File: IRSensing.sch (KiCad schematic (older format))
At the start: 0 parts

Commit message: Adding IR Sensor
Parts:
- added R11, R12: R, symbol R
- added U3: OPB733TR, Custom:OPB733TR, symbol OPB733TR
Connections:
- new net: R12.1, U3.4 (AN)
- new net +5V: R11.2, R12.2
- new net GND: U3.1 (CAT), U3.2 (E)
- new net Vout_IR: R11.1, U3.3 (C)
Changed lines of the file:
@@
 Comment4 ""
 $EndDescr
+$Comp
+L OPB733TR U3
+U 1 1 5AA80AD0
+P 5600 3350
+F 0 "U3" H 5600 3050 60  0000 C CNN
+F 1 "OPB733TR" H 5600 3650 60  0000 C CNN
+F 2 "Custom:OPB733TR" H 5500 2950 60  0001 C CNN
+F 3 "http://www.ttelectronics.com/sites/default/files/download-files/OPB733TR.pdf" H 5600 2950 60  0001 C CNN
+	1    5600 3350
+	-1   0    0    1
+$EndComp
+Wire Wire Line
+	6150 3450 6350 3450
+Wire Wire Line
+	6350 3450 6350 3000
+Wire Wire Line
+	6150 3250 6350 3250
+Connection ~ 6350 3250
+$Comp
+L R R11
+U 1 1 5AA80B31
+P 4750 3250
+F 0 "R11" V 4830 3250 50  0000 C CNN
+F 1 "R" V 4750 3250 50  0000 C CNN
+F 2 "" V 4680 3250 50  0001 C CNN
+F 3 "" H 4750 3250 50  0001 C CNN
+	1    4750 3250
+	0    1    1    0
+$EndComp
+$Comp
+L R R12
+U 1 1 5AA80B73
+P 4750 3450
+F 0 "R12" V 4830 3450 50  0000 C CNN
+F 1 "R" V 4750 3450 50  0000 C CNN
+F 2 "" V 4680 3450 50  0001 C CNN
+F 3 "" H 4750 3450 50  0001 C CNN
+	1    4750 3450
+	0    1    1    0
+$EndComp
+Wire Wire Line
+	4900 3250 5050 3250
+Wire Wire Line
+	5050 3450 4900 3450
+Wire Wire Line
+	4600 3450 4350 3450
+Wire Wire Line
+	4350 3450 4350 3000
+Wire Wire Line
+	4350 3250 4600 3250
+Connection ~ 4350 3250
+$Comp
+L +5V #PWR017
+U 1 1 5AA80C09
+P 4350 3000
+F 0 "#PWR017" H 4350 2850 50  0001 C CNN
+F 1 "+5V" H 4350 3140 50  0000 C CNN
+F 2 "" H 4350 3000 50  0001 C CNN
+F 3 "" H 4350 3000 50  0001 C CNN
+	1    4350 3000
+	1    0    0    -1
+$EndComp
+$Comp
+L GND #PWR018
+U 1 1 5AA80C23
+P 6350 3000
+F 0 "#PWR018" H 6350 2750 50  0001 C CNN
+F 1 "GND" H 6350 2850 50  0000 C CNN
+F 2 "" H 6350 3000 50  0001 C CNN
+F 3 "" H 6350 3000 50  0001 C CNN
+	1    6350 3000
+	-1   0    0    1
+$EndComp
+Text HLabel 5000 3100 1    60   Output Italic 0
+Vout_IR
+Wire Wire Line
+	5000 3100 5000 3250
+Connection ~ 5000 3250
 $EndSCHEMATC

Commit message: Finished Schematic
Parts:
- added J? (x8): Conn_01x03, symbol Conn_01x03
- added Q?: Q_NPN_BEC, symbol Q_NPN_BEC
- added R? (x3): 30k, symbol R
- added R? (x3): 36, symbol R
- added U? (x3): OPB733TR, Custom:OPB733TR, symbol OPB733TR
- R?: renamed from R11; value R -> 30k
- R?: renamed from R12; value R -> 36
- renumbered U3 to U?
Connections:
- net GND: now also J?.1 (Pin_1), J?.1 (Pin_1), J?.1 (Pin_1), J?.1 (Pin_1); no longer U?.1 (CAT), U?.2 (E)
- net +5V renamed 3V3_C1
- net 3V3_C1: now also J?.2 (Pin_2)
- net Vout_IR renamed Vout_IR_C1
- net Vout_IR_C1: now also J?.3 (Pin_3)
- new net: R?.1, U?.4 (AN) (x3)
- new net +3V3: Q?.3 (C)
- new net 3V3_C2: J?.2 (Pin_2), R?.2, R?.2
- new net 3V3_C3: J?.2 (Pin_2), R?.2, R?.2
- new net 3V3_C4: J?.2 (Pin_2), R?.2, R?.2
- new net D_Power: J?.2 (Pin_2), J?.2 (Pin_2), J?.2 (Pin_2), J?.2 (Pin_2), Q?.2 (E)
- new net D_SIG: Q?.1 (B)
- new net GND_C1: J?.1 (Pin_1), U?.1 (CAT), U?.2 (E)
- new net GND_C2: J?.1 (Pin_1), U?.1 (CAT), U?.2 (E)
- new net GND_C3: J?.1 (Pin_1), U?.1 (CAT), U?.2 (E)
- new net GND_C4: J?.1 (Pin_1), U?.1 (CAT), U?.2 (E)
- new net Vout_IR_1: J?.3 (Pin_3)
- new net Vout_IR_2: J?.3 (Pin_3)
- new net Vout_IR_3: J?.3 (Pin_3)
- new net Vout_IR_4: J?.3 (Pin_3)
- new net Vout_IR_C2: J?.3 (Pin_3), R?.1, U?.3 (C)
- new net Vout_IR_C3: J?.3 (Pin_3), R?.1, U?.3 (C)
- new net Vout_IR_C4: J?.3 (Pin_3), R?.1, U?.3 (C)
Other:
- note added: "Diode Power"
- note added: "IR Boards"
- note added: "Main Board"
- moved on the sheet: R?, U?

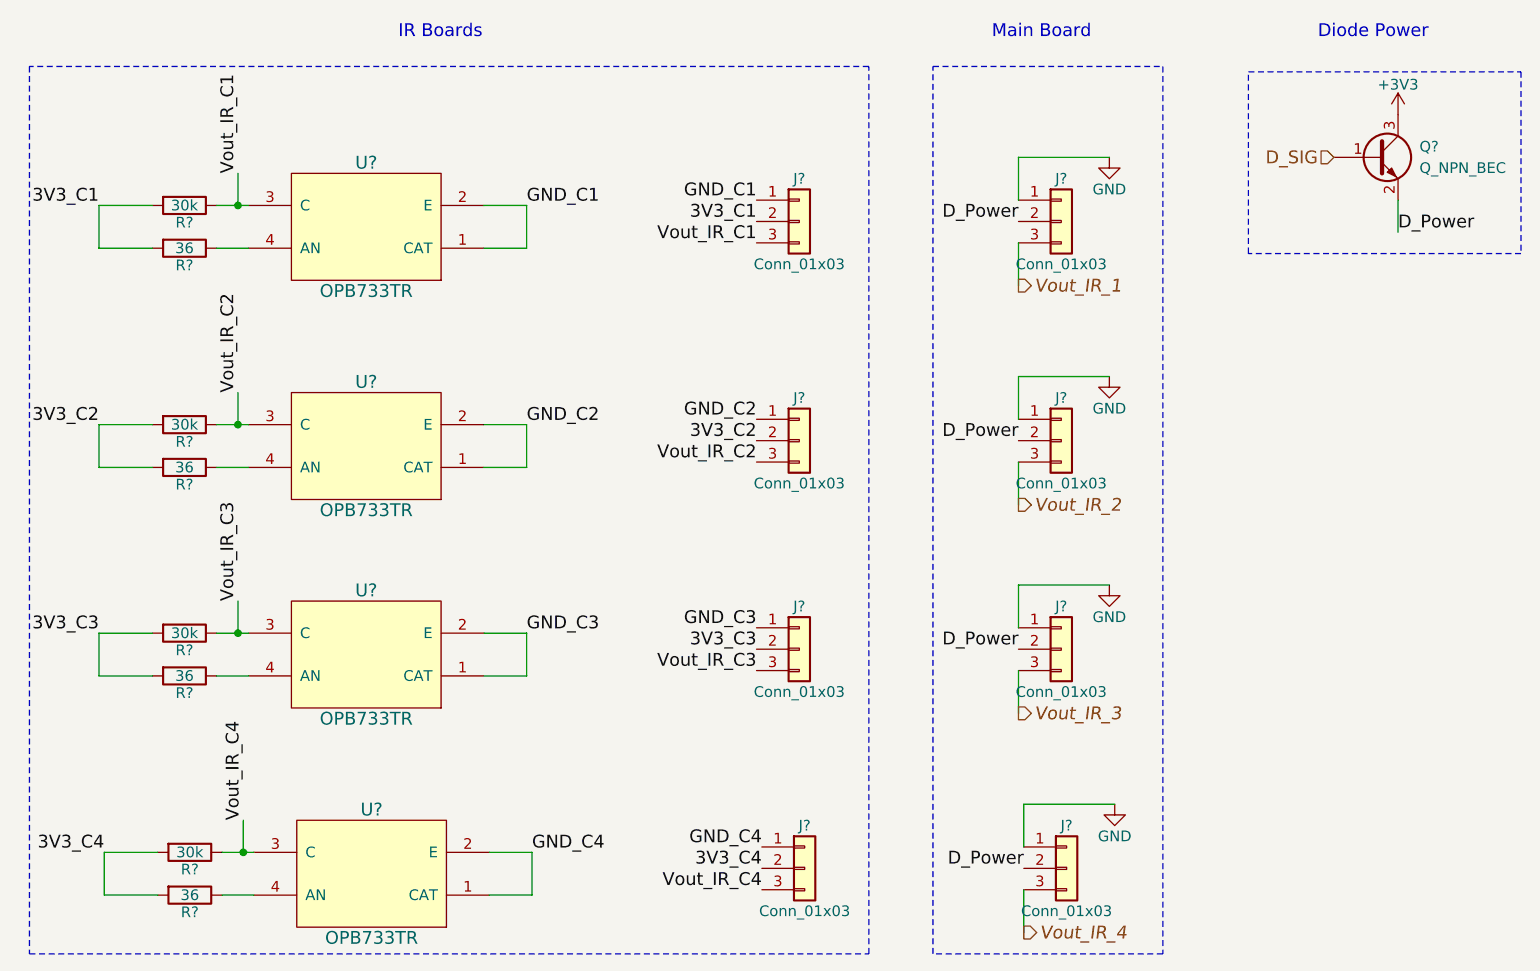
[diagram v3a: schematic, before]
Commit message: Started associating footprints
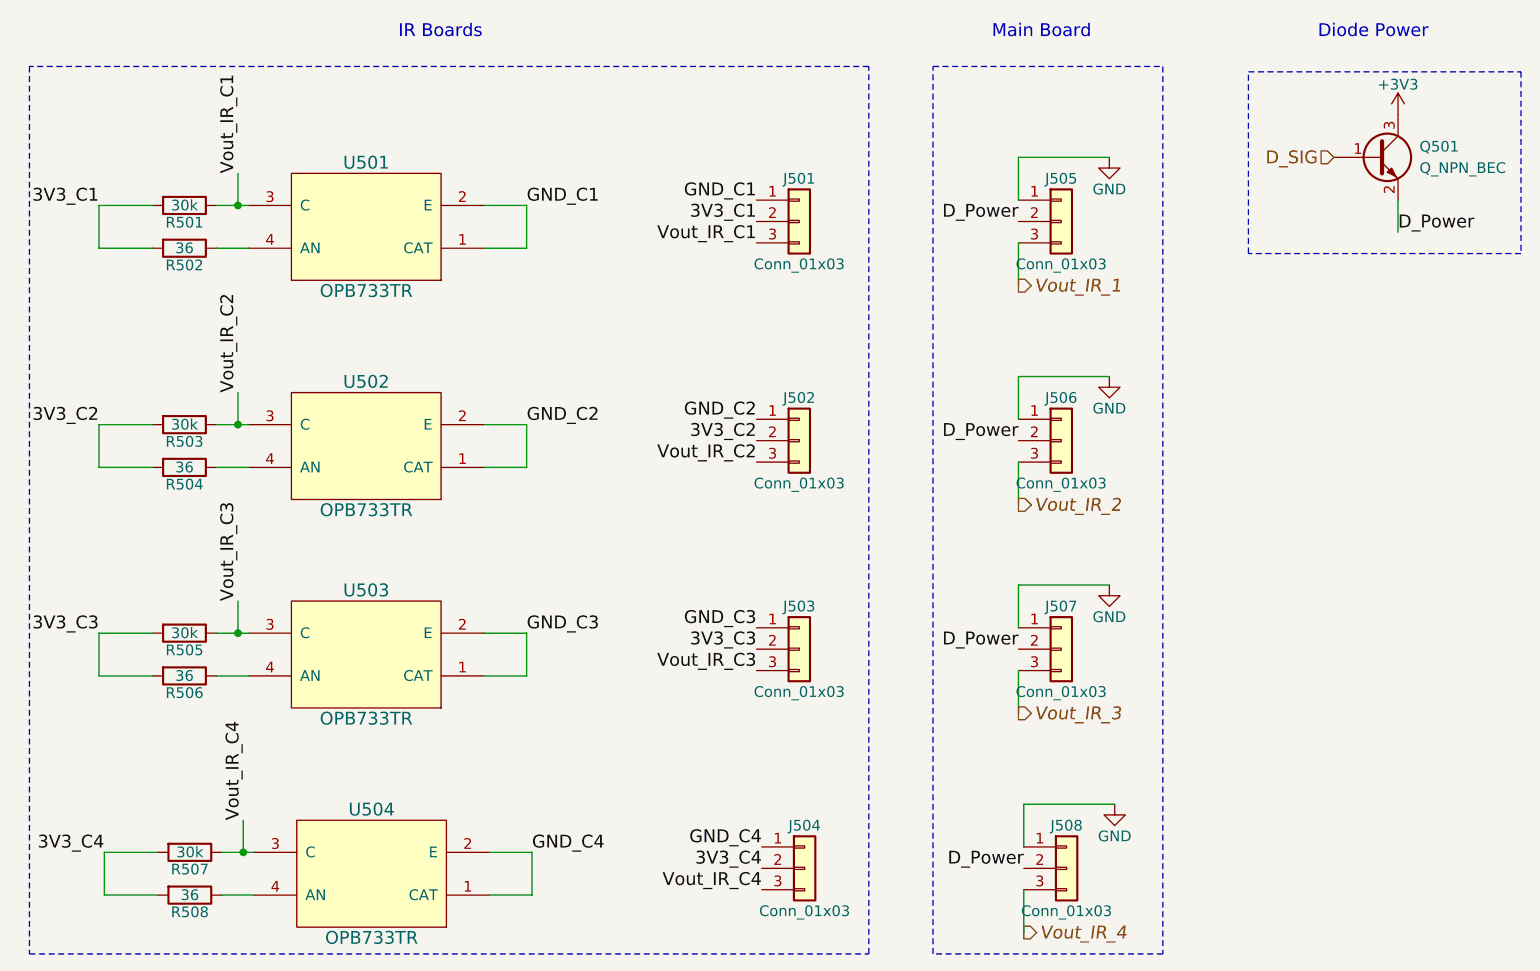
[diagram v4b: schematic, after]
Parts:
- J501, J502, J503, J504, J505, J506, J507, J508: renamed from J?; footprint (none) -> Pin_Headers:Pin_Header_Angled_1x03_Pitch1.27mm
- gave numbers to parts that had none: 13
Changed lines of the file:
@@
 $EndDescr
 $Comp
-L OPB733TR U?
+L OPB733TR U501
 U 1 1 5AA80AD0
 P 3125 2125
-F 0 "U?" H 3125 1825 60  0000 C CNN
+F 0 "U501" H 3125 1825 60  0000 C CNN
 F 1 "OPB733TR" H 3125 2425 60  0000 C CNN
 F 2 "Custom:OPB733TR" H 3025 1725 60  0001 C CNN
@@
 	3675 2025 3875 2025
 $Comp
-L R R?
+L R R501
 U 1 1 5AA80B31
 P 2275 2025
-F 0 "R?" V 2355 2025 50  0000 C CNN
+F 0 "R501" V 2355 2025 50  0000 C CNN
 F 1 "30k" V 2275 2025 50  0000 C CNN
 F 2 "" V 2205 2025 50  0001 C CNN
@@
 $EndComp
 $Comp
-L R R?
+L R R502
 U 1 1 5AA80B73
 P 2275 2225
-F 0 "R?" V 2355 2225 50  0000 C CNN
+F 0 "R502" V 2355 2225 50  0000 C CNN
 F 1 "36" V 2275 2225 50  0000 C CNN
 F 2 "" V 2205 2225 50  0001 C CNN
@@
 	1875 2025 2125 2025
 $Comp
-L GND #PWR018
+L GND #PWR029
 U 1 1 5AA80C23
 P 6600 1800
-F 0 "#PWR018" H 6600 1550 50  0001 C CNN
+F 0 "#PWR029" H 6600 1550 50  0001 C CNN
 F 1 "GND" H 6600 1650 50  0000 C CNN
 F 2 "" H 6600 1800 50  0001 C CNN
@@
 Connection ~ 2525 2025
 $Comp
-L Conn_01x03 J?
+L Conn_01x03 J501
 U 1 1 5AC5CFBC
 P 5150 2100
-F 0 "J?" H 5150 2300 50  0000 C CNN
+F 0 "J501" H 5150 2300 50  0000 C CNN
 F 1 "Conn_01x03" H 5150 1900 50  0000 C CNN
-F 2 "" H 5150 2100 50  0001 C CNN
+F 2 "Pin_Headers:Pin_Header_Angled_1x03_Pitch1.27mm" H 5150 2100 50  0001 C CNN
 F 3 "" H 5150 2100 50  0001 C CNN
 	1    5150 2100
@@
 3V3_C1
 $Comp
-L Conn_01x03 J?
+L Conn_01x03 J505
 U 1 1 5AC5E221
 P 6375 2100
-F 0 "J?" H 6375 2300 50  0000 C CNN
+F 0 "J505" H 6375 2300 50  0000 C CNN
 F 1 "Conn_01x03" H 6375 1900 50  0000 C CNN
-F 2 "" H 6375 2100 50  0001 C CNN
+F 2 "Pin_Headers:Pin_Header_Angled_1x03_Pitch1.27mm" H 6375 2100 50  0001 C CNN
 F 3 "" H 6375 2100 50  0001 C CNN
 	1    6375 2100
@@
 	1875 2225 1875 2025
 $Comp
-L OPB733TR U?
+L OPB733TR U502
 U 1 1 5AC5EDE3
 P 3125 3150
-F 0 "U?" H 3125 2850 60  0000 C CNN
+F 0 "U502" H 3125 2850 60  0000 C CNN
 F 1 "OPB733TR" H 3125 3450 60  0000 C CNN
 F 2 "Custom:OPB733TR" H 3025 2750 60  0001 C CNN
@@
 	3675 3050 3875 3050
 $Comp
-L R R?
+L R R503
 U 1 1 5AC5EDEB
 P 2275 3050
-F 0 "R?" V 2355 3050 50  0000 C CNN
+F 0 "R503" V 2355 3050 50  0000 C CNN
 F 1 "30k" V 2275 3050 50  0000 C CNN
 F 2 "" V 2205 3050 50  0001 C CNN
@@
 $EndComp
 $Comp
-L R R?
+L R R504
 U 1 1 5AC5EDF1
 P 2275 3250
-F 0 "R?" V 2355 3250 50  0000 C CNN
+F 0 "R504" V 2355 3250 50  0000 C CNN
 F 1 "36" V 2275 3250 50  0000 C CNN
 F 2 "" V 2205 3250 50  0001 C CNN
@@
 	1875 3050 2125 3050
 $Comp
-L GND #PWR?
+L GND #PWR030
 U 1 1 5AC5EDFB
 P 6600 2825
-F 0 "#PWR?" H 6600 2575 50  0001 C CNN
+F 0 "#PWR030" H 6600 2575 50  0001 C CNN
 F 1 "GND" H 6600 2675 50  0000 C CNN
 F 2 "" H 6600 2825 50  0001 C CNN
@@
 Connection ~ 2525 3050
 $Comp
-L Conn_01x03 J?
+L Conn_01x03 J502
 U 1 1 5AC5EE0A
 P 5150 3125
-F 0 "J?" H 5150 3325 50  0000 C CNN
+F 0 "J502" H 5150 3325 50  0000 C CNN
 F 1 "Conn_01x03" H 5150 2925 50  0000 C CNN
-F 2 "" H 5150 3125 50  0001 C CNN
+F 2 "Pin_Headers:Pin_Header_Angled_1x03_Pitch1.27mm" H 5150 3125 50  0001 C CNN
 F 3 "" H 5150 3125 50  0001 C CNN
 	1    5150 3125
@@
 3V3_C2
 $Comp
-L Conn_01x03 J?
+L Conn_01x03 J506
 U 1 1 5AC5EE16
 P 6375 3125
-F 0 "J?" H 6375 3325 50  0000 C CNN
+F 0 "J506" H 6375 3325 50  0000 C CNN
 F 1 "Conn_01x03" H 6375 2925 50  0000 C CNN
-F 2 "" H 6375 3125 50  0001 C CNN
+F 2 "Pin_Headers:Pin_Header_Angled_1x03_Pitch1.27mm" H 6375 3125 50  0001 C CNN
 F 3 "" H 6375 3125 50  0001 C CNN
 	1    6375 3125
@@
 	1875 3250 1875 3050
 $Comp
-L OPB733TR U?
+L OPB733TR U503
 U 1 1 5AC5EFD0
 P 3125 4125
-F 0 "U?" H 3125 3825 60  0000 C CNN
+F 0 "U503" H 3125 3825 60  0000 C CNN
 F 1 "OPB733TR" H 3125 4425 60  0000 C CNN
 F 2 "Custom:OPB733TR" H 3025 3725 60  0001 C CNN
@@
 	3675 4025 3875 4025
 $Comp
-L R R?
+L R R505
 U 1 1 5AC5EFD8
 P 2275 4025
-F 0 "R?" V 2355 4025 50  0000 C CNN
+F 0 "R505" V 2355 4025 50  0000 C CNN
 F 1 "30k" V 2275 4025 50  0000 C CNN
 F 2 "" V 2205 4025 50  0001 C CNN
@@
 $EndComp
 $Comp
-L R R?
+L R R506
 U 1 1 5AC5EFDE
 P 2275 4225
-F 0 "R?" V 2355 4225 50  0000 C CNN
+F 0 "R506" V 2355 4225 50  0000 C CNN
 F 1 "36" V 2275 4225 50  0000 C CNN
 F 2 "" V 2205 4225 50  0001 C CNN
@@
 	1875 4025 2125 4025
 $Comp
-L GND #PWR?
+L GND #PWR031
 U 1 1 5AC5EFE8
 P 6600 3800
-F 0 "#PWR?" H 6600 3550 50  0001 C CNN
+F 0 "#PWR031" H 6600 3550 50  0001 C CNN
 F 1 "GND" H 6600 3650 50  0000 C CNN
 F 2 "" H 6600 3800 50  0001 C CNN
@@
 Connection ~ 2525 4025
 $Comp
-L Conn_01x03 J?
+L Conn_01x03 J503
 U 1 1 5AC5EFF7
 P 5150 4100
-F 0 "J?" H 5150 4300 50  0000 C CNN
+F 0 "J503" H 5150 4300 50  0000 C CNN
 F 1 "Conn_01x03" H 5150 3900 50  0000 C CNN
-F 2 "" H 5150 4100 50  0001 C CNN
+F 2 "Pin_Headers:Pin_Header_Angled_1x03_Pitch1.27mm" H 5150 4100 50  0001 C CNN
 F 3 "" H 5150 4100 50  0001 C CNN
 	1    5150 4100
@@
 3V3_C3
 $Comp
-L Conn_01x03 J?
+L Conn_01x03 J507
 U 1 1 5AC5F003
 P 6375 4100
-F 0 "J?" H 6375 4300 50  0000 C CNN
+F 0 "J507" H 6375 4300 50  0000 C CNN
 F 1 "Conn_01x03" H 6375 3900 50  0000 C CNN
-F 2 "" H 6375 4100 50  0001 C CNN
+F 2 "Pin_Headers:Pin_Header_Angled_1x03_Pitch1.27mm" H 6375 4100 50  0001 C CNN
 F 3 "" H 6375 4100 50  0001 C CNN
 	1    6375 4100
@@
 	1875 4225 1875 4025
 $Comp
-L OPB733TR U?
+L OPB733TR U504
 U 1 1 5AC5F0CD
 P 3150 5150
-F 0 "U?" H 3150 4850 60  0000 C CNN
+F 0 "U504" H 3150 4850 60  0000 C CNN
 F 1 "OPB733TR" H 3150 5450 60  0000 C CNN
 F 2 "Custom:OPB733TR" H 3050 4750 60  0001 C CNN
@@
 	3700 5050 3900 5050
 $Comp
-L R R?
+L R R507
 U 1 1 5AC5F0D5
 P 2300 5050
-F 0 "R?" V 2380 5050 50  0000 C CNN
+F 0 "R507" V 2380 5050 50  0000 C CNN
 F 1 "30k" V 2300 5050 50  0000 C CNN
 F 2 "" V 2230 5050 50  0001 C CNN
@@
 $EndComp
 $Comp
-L R R?
+L R R508
 U 1 1 5AC5F0DB
 P 2300 5250
-F 0 "R?" V 2380 5250 50  0000 C CNN
+F 0 "R508" V 2380 5250 50  0000 C CNN
 F 1 "36" V 2300 5250 50  0000 C CNN
 F 2 "" V 2230 5250 50  0001 C CNN
@@
 	1900 5050 2150 5050
 $Comp
-L GND #PWR?
+L GND #PWR032
 U 1 1 5AC5F0E5
 P 6625 4825
-F 0 "#PWR?" H 6625 4575 50  0001 C CNN
+F 0 "#PWR032" H 6625 4575 50  0001 C CNN
 F 1 "GND" H 6625 4675 50  0000 C CNN
 F 2 "" H 6625 4825 50  0001 C CNN
@@
 Connection ~ 2550 5050
 $Comp
-L Conn_01x03 J?
+L Conn_01x03 J504
 U 1 1 5AC5F0F4
 P 5175 5125
-F 0 "J?" H 5175 5325 50  0000 C CNN
+F 0 "J504" H 5175 5325 50  0000 C CNN
 F 1 "Conn_01x03" H 5175 4925 50  0000 C CNN
-F 2 "" H 5175 5125 50  0001 C CNN
+F 2 "Pin_Headers:Pin_Header_Angled_1x03_Pitch1.27mm" H 5175 5125 50  0001 C CNN
 F 3 "" H 5175 5125 50  0001 C CNN
 	1    5175 5125
@@
 3V3_C4
 $Comp
-L Conn_01x03 J?
+L Conn_01x03 J508
 U 1 1 5AC5F100
 P 6400 5125
-F 0 "J?" H 6400 5325 50  0000 C CNN
+F 0 "J508" H 6400 5325 50  0000 C CNN
 F 1 "Conn_01x03" H 6400 4925 50  0000 C CNN
-F 2 "" H 6400 5125 50  0001 C CNN
+F 2 "Pin_Headers:Pin_Header_Angled_1x03_Pitch1.27mm" H 6400 5125 50  0001 C CNN
 F 3 "" H 6400 5125 50  0001 C CNN
 	1    6400 5125
@@
 Main Board
 $Comp
-L Q_NPN_BEC Q?
+L Q_NPN_BEC Q501
 U 1 1 5AC96FCA
 P 7850 1800
-F 0 "Q?" H 8050 1850 50  0000 L CNN
+F 0 "Q501" H 8050 1850 50  0000 L CNN
 F 1 "Q_NPN_BEC" H 8050 1750 50  0000 L CNN
 F 2 "" H 8050 1900 50  0001 C CNN
@@
 D_SIG
 $Comp
-L +3V3 #PWR?
+L +3V3 #PWR033
 U 1 1 5AC9715B
 P 7950 1600
-F 0 "#PWR?" H 7950 1450 50  0001 C CNN
+F 0 "#PWR033" H 7950 1450 50  0001 C CNN
 F 1 "+3V3" H 7950 1740 50  0000 C CNN
 F 2 "" H 7950 1600 50  0001 C CNN
